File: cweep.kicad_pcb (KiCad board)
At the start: 2 copper layers, 106.6 x 82.7 mm, 57 parts

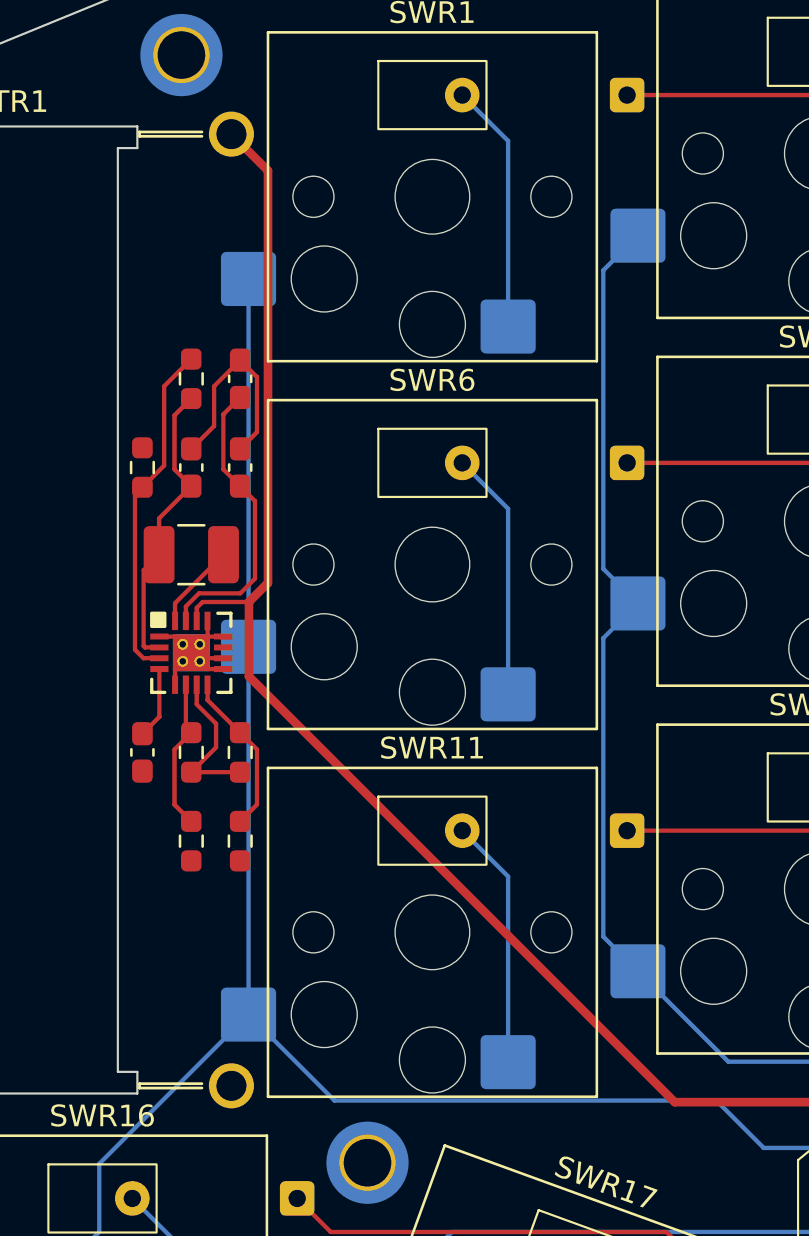
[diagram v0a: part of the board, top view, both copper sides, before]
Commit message: feat: add solar cell connectors
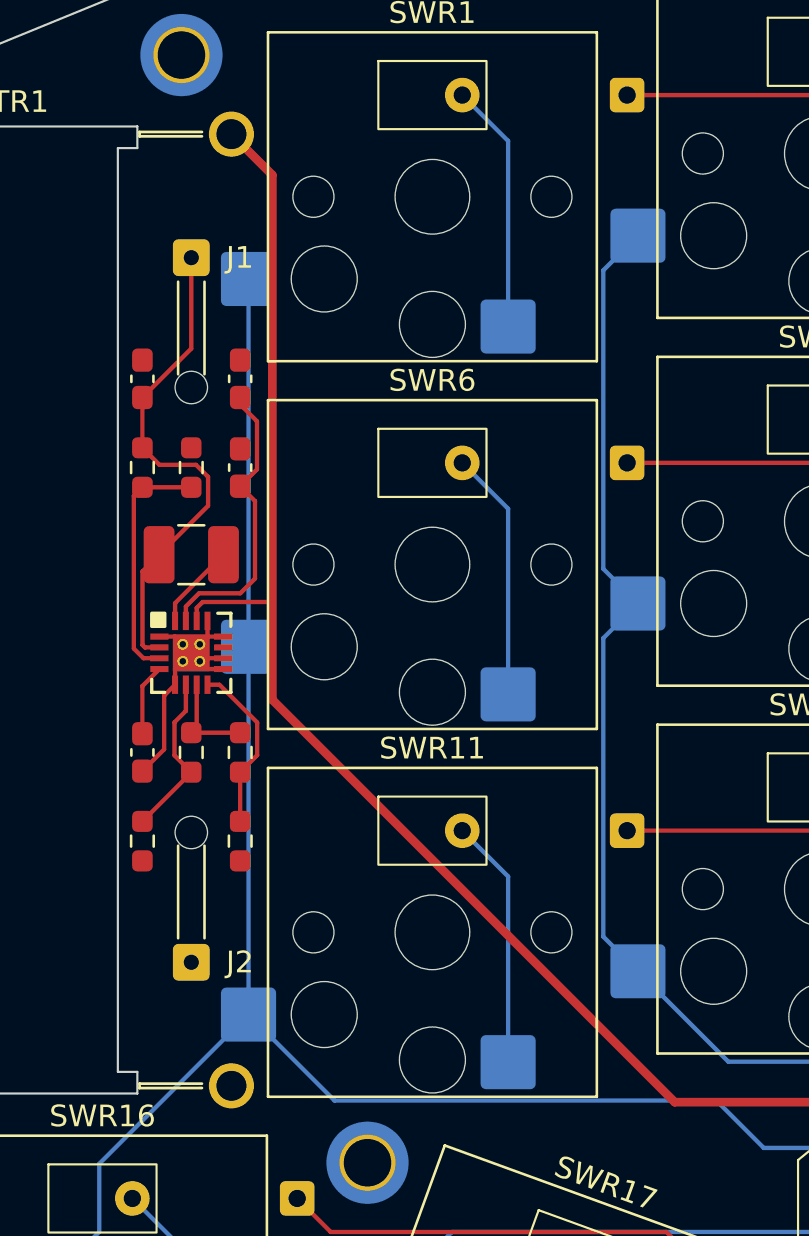
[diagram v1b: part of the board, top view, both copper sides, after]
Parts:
- added J1: 24AWG Hole, Connector_Wire:SolderWire-0.127sqmm_1x01_D0.48mm_OD1mm_Relief, F.Cu at (175.9, 53.8)
- added J2: 24AWG Hole, Connector_Wire:SolderWire-0.127sqmm_1x01_D0.48mm_OD1mm_Relief, F.Cu at (175.9, 86.4)
- moved CHVR1 4.68 mm to (173.6, 59.4)
- moved ROCR2 4.68 mm to (173.6, 63.5), turned to 90 degrees
- moved ROCR1 2.26 mm to (175.9, 63.5)
- moved ROVR1 2.26 mm to (173.6, 80.8)
- turned ROVR2 to 90 degrees
- turned RUVR2 to 90 degrees
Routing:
- net Net-(J1-Pin_1): track 13.7 -> 23.2 mm
- net GND: track 17.1 -> 11.5 mm
- net Net-(UR2-VOC_SAMP): track 15.8 -> 11.2 mm
- net Net-(UR2-VRDIV): track 7.15 -> 4.58 mm
- net Net-(UR2-VBAT_OV): track 7.06 -> 7.79 mm

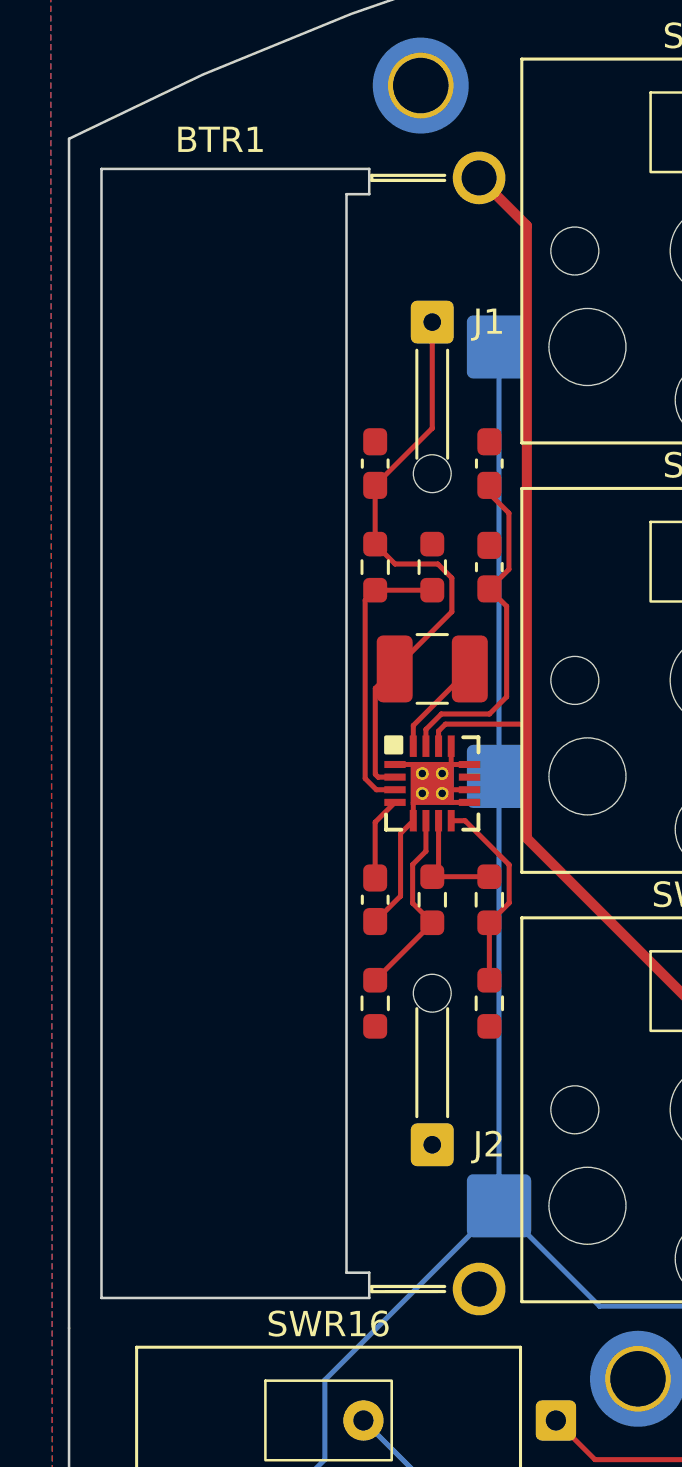
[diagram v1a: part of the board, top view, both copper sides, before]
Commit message: fix: AAA -> 10440
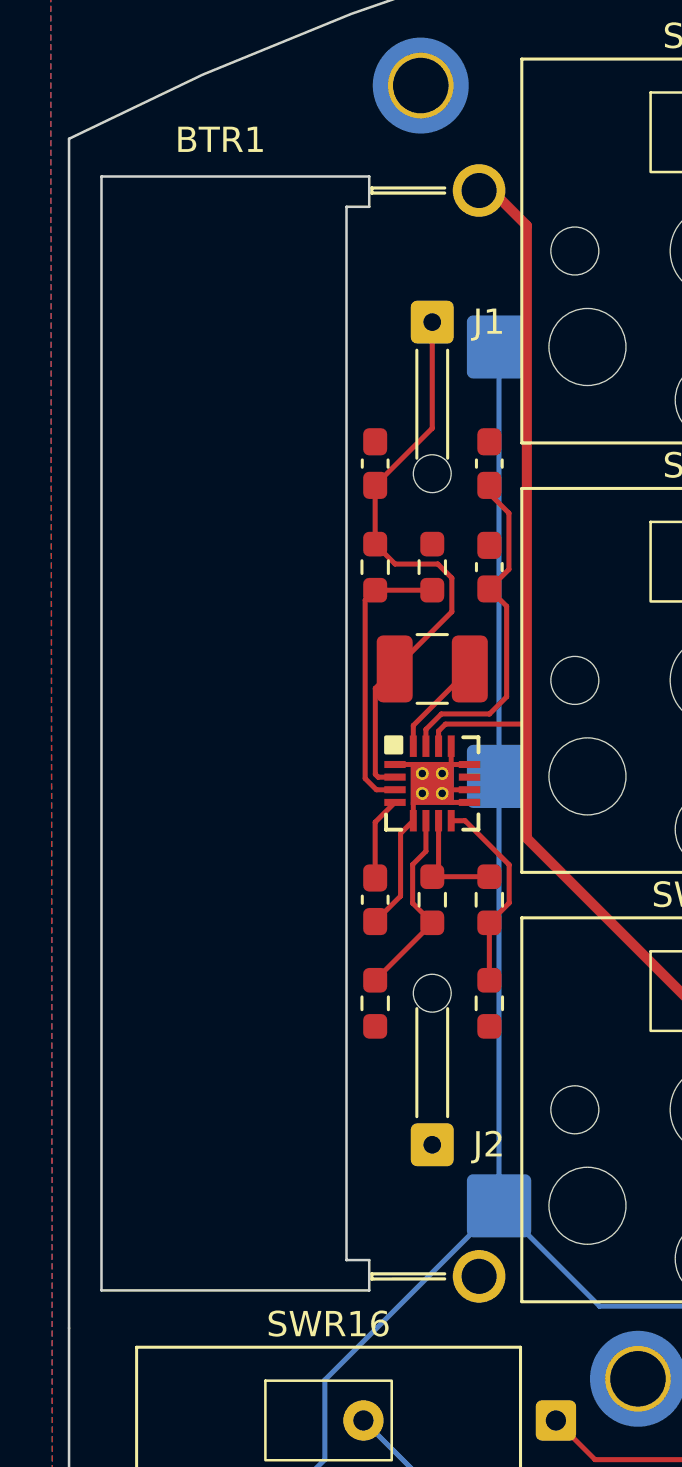
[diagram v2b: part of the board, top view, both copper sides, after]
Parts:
- BTR1: value BATTERY LITH-ION 3.7V AAA -> 10440; footprint com_snapeda_Keystone:BatteryHolder_Keystone_230-1_1xAAA -> com_snapeda_Keystone:BatteryHolder_Keystone_230-1_1x10440

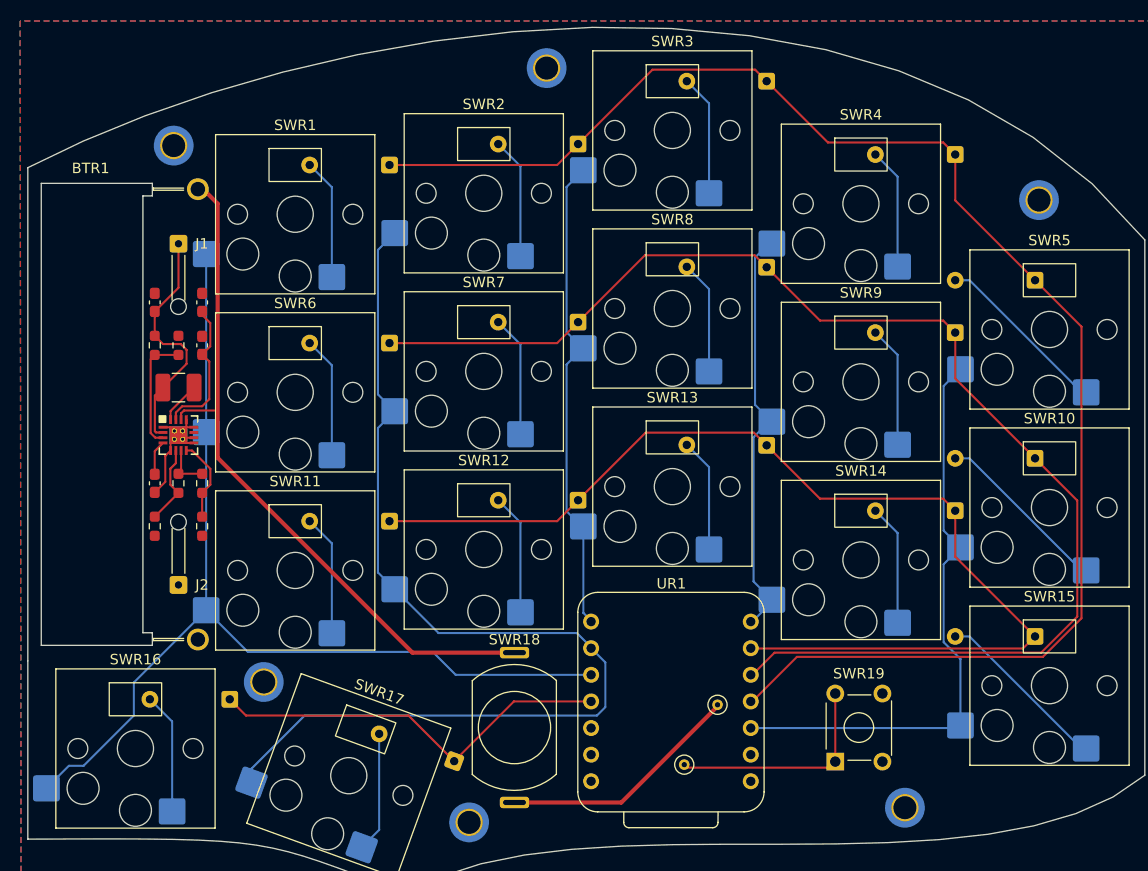
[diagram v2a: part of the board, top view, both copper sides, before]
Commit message: refactor: normalize labels and organize schematic
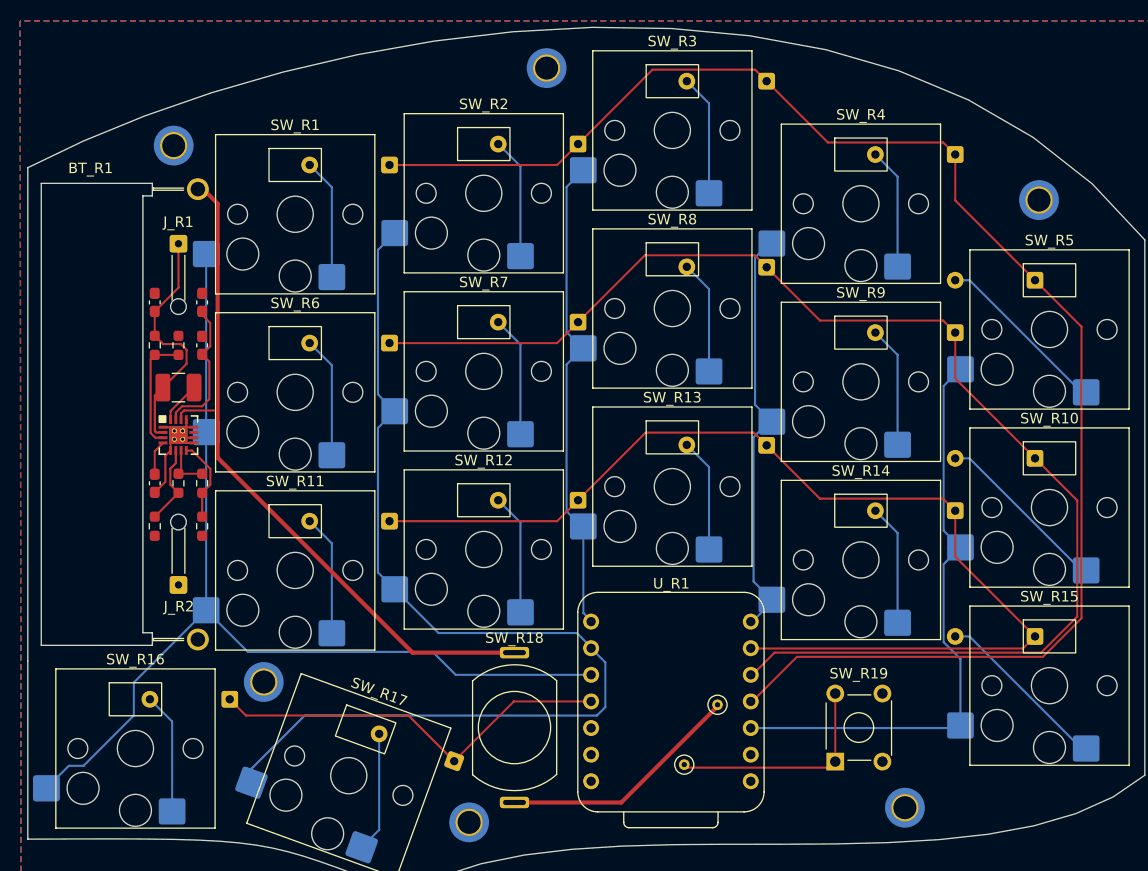
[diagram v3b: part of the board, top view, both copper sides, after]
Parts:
- turned SW_R18 to 180 degrees
- renumbered BTR1 to BT_R1, CBYPR1 to CBYP_R1, CHVR1 to CHV_R1, CREFR1 to CREF_R1, CSTORR1 to CSTOR_R1, DR1 to D_R1, DR10 to D_R10, DR11 to D_R11, DR12 to D_R12, DR13 to D_R13, DR14 to D_R14, DR15 to D_R15, DR16 to D_R16, DR17 to D_R17, DR2 to D_R2, DR3 to D_R3, DR4 to D_R4, DR5 to D_R5, DR6 to D_R6, DR7 to D_R7, DR8 to D_R8, DR9 to D_R9, H1 to H_R1, H2 to H_R2, H3 to H_R3, H4 to H_R4, H5 to H_R5, H6 to H_R6, J1 to J_R1, J2 to J_R2, LBSTR1 to LBST_R1, ROCR1 to ROC_R1, ROCR2 to ROC_R2, ROVR1 to ROV_R1, ROVR2 to ROV_R2, RUVR1 to RUV_R1, RUVR2 to RUV_R2, SCR1 to SC_R1, SWR1 to SW_R1, SWR10 to SW_R10, SWR11 to SW_R11, SWR12 to SW_R12, SWR13 to SW_R13, SWR14 to SW_R14, SWR15 to SW_R15, SWR16 to SW_R16, SWR17 to SW_R17, SWR18 to SW_R18, SWR19 to SW_R19, SWR2 to SW_R2, SWR3 to SW_R3, SWR4 to SW_R4, SWR5 to SW_R5, SWR6 to SW_R6, SWR7 to SW_R7, SWR8 to SW_R8, SWR9 to SW_R9, UR1 to U_R1, UR2 to U_R2
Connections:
- net /column r0 renamed /COL_R0
- net /column r1 renamed /COL_R1
- net /column r2 renamed /COL_R2
- net /column r3 renamed /COL_R3
- net /column r4 renamed /COL_R4
- net /row r0 renamed /ROW_R0
- net /row r1 renamed /ROW_R1
- net /row r2 renamed /ROW_R2
- net /row r3 renamed /ROW_R3
- net Net-(J1-Pin_1) renamed /SOL_R
- net Net-(UR1-RESET) renamed /RST_R
- BT_R1 pad 1: /VBATR -> /VBAT_R
- SW_R18 pad 1: Net-(SWR18-A) -> /VBAT_R
- SW_R18 pad 2: /VBATR -> /BAT_R
- U_R1 pad 15: Net-(SWR18-A) -> /BAT_R
- U_R2 pad 14: /VBATR -> /VBAT_R
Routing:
- net /VBAT_R: track 0.00 -> 67.2 mm
- net /VBATR: track 67.2 -> 0.00 mm
- net Net-(SWR18-A): track 23.3 -> 0.00 mm
- net /BAT_R: track 0.00 -> 23.3 mm

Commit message: feat: make keyboard switch reversible
* fix: use SMD diode to accommodate reversible switch
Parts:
- added JP1: SolderJumper_3_Open, cweep:SolderJumper-3_P2.0mm_Open_TrianglePad1.0x1.5mm_Reversible, F.Cu at (79.3, 84.7)
- added JP10: SolderJumper_3_Open, cweep:SolderJumper-3_P2.0mm_Open_TrianglePad1.0x1.5mm_Reversible, F.Cu at (69.2, 74.6)
- added JP11: SolderJumper_3_Open, cweep:SolderJumper-3_P2.0mm_Open_TrianglePad1.0x1.5mm_Reversible, F.Cu at (72.3, 77.1)
- added JP12: SolderJumper_3_Open, cweep:SolderJumper-3_P2.0mm_Open_TrianglePad1.0x1.5mm_Reversible, F.Cu at (69.2, 79.6)
- added JP13: SolderJumper_3_Open, cweep:SolderJumper-3_P2.0mm_Open_TrianglePad1.0x1.5mm_Reversible, F.Cu at (69.2, 82.2)
- added JP14: SolderJumper_3_Open, cweep:SolderJumper-3_P2.0mm_Open_TrianglePad1.0x1.5mm_Reversible, F.Cu at (69.2, 84.7)
- added JP2: SolderJumper_3_Open, cweep:SolderJumper-3_P2.0mm_Open_TrianglePad1.0x1.5mm_Reversible, F.Cu at (79.3, 82.2)
- added JP3: SolderJumper_3_Open, cweep:SolderJumper-3_P2.0mm_Open_TrianglePad1.0x1.5mm_Reversible, F.Cu at (79.3, 79.6)
- added JP4: SolderJumper_3_Open, cweep:SolderJumper-3_P2.0mm_Open_TrianglePad1.0x1.5mm_Reversible, F.Cu at (76.3, 77.1)
- added JP5: SolderJumper_3_Open, cweep:SolderJumper-3_P2.0mm_Open_TrianglePad1.0x1.5mm_Reversible, F.Cu at (79.3, 74.6)
- added JP6: SolderJumper_3_Open, cweep:SolderJumper-3_P2.0mm_Open_TrianglePad1.0x1.5mm_Reversible, F.Cu at (79.3, 72.0)
- added JP7: SolderJumper_3_Open, cweep:SolderJumper-3_P2.0mm_Open_TrianglePad1.0x1.5mm_Reversible, F.Cu at (79.3, 69.5)
- added JP8: SolderJumper_3_Open, cweep:SolderJumper-3_P2.0mm_Open_TrianglePad1.0x1.5mm_Reversible, F.Cu at (69.2, 69.5)
- added JP9: SolderJumper_3_Open, cweep:SolderJumper-3_P2.0mm_Open_TrianglePad1.0x1.5mm_Reversible, F.Cu at (69.2, 72.0)
- D1: renamed from D_R1; value 1N4148 -> 1N4148W; footprint Diode_THT:D_DO-35_SOD27_P7.62mm_Horizontal -> cweep:D_SOD-123_Reversible; moved to F.Cu
- D10: renamed from D_R10; value 1N4148 -> 1N4148W; footprint Diode_THT:D_DO-35_SOD27_P7.62mm_Horizontal -> cweep:D_SOD-123_Reversible; moved to F.Cu
- D11: renamed from D_R11; value 1N4148 -> 1N4148W; footprint Diode_THT:D_DO-35_SOD27_P7.62mm_Horizontal -> cweep:D_SOD-123_Reversible; moved to F.Cu
- D12: renamed from D_R12; value 1N4148 -> 1N4148W; footprint Diode_THT:D_DO-35_SOD27_P7.62mm_Horizontal -> cweep:D_SOD-123_Reversible; moved to F.Cu
- D13: renamed from D_R13; value 1N4148 -> 1N4148W; footprint Diode_THT:D_DO-35_SOD27_P7.62mm_Horizontal -> cweep:D_SOD-123_Reversible; moved to F.Cu
- D14: renamed from D_R14; value 1N4148 -> 1N4148W; footprint Diode_THT:D_DO-35_SOD27_P7.62mm_Horizontal -> cweep:D_SOD-123_Reversible; moved to F.Cu
- D15: renamed from D_R15; value 1N4148 -> 1N4148W; footprint Diode_THT:D_DO-35_SOD27_P7.62mm_Horizontal -> cweep:D_SOD-123_Reversible; moved to F.Cu
- D16: renamed from D_R16; value 1N4148 -> 1N4148W; footprint Diode_THT:D_DO-35_SOD27_P7.62mm_Horizontal -> cweep:D_SOD-123_Reversible; moved to F.Cu
- D17: renamed from D_R17; value 1N4148 -> 1N4148W; footprint Diode_THT:D_DO-35_SOD27_P7.62mm_Horizontal -> cweep:D_SOD-123_Reversible; moved to F.Cu
- D2: renamed from D_R2; value 1N4148 -> 1N4148W; footprint Diode_THT:D_DO-35_SOD27_P7.62mm_Horizontal -> cweep:D_SOD-123_Reversible; moved to F.Cu
- D3: renamed from D_R3; value 1N4148 -> 1N4148W; footprint Diode_THT:D_DO-35_SOD27_P7.62mm_Horizontal -> cweep:D_SOD-123_Reversible; moved to F.Cu
- D4: renamed from D_R4; value 1N4148 -> 1N4148W; footprint Diode_THT:D_DO-35_SOD27_P7.62mm_Horizontal -> cweep:D_SOD-123_Reversible; moved to F.Cu
- D5: renamed from D_R5; value 1N4148 -> 1N4148W; footprint Diode_THT:D_DO-35_SOD27_P7.62mm_Horizontal -> cweep:D_SOD-123_Reversible; moved to F.Cu
- D6: renamed from D_R6; value 1N4148 -> 1N4148W; footprint Diode_THT:D_DO-35_SOD27_P7.62mm_Horizontal -> cweep:D_SOD-123_Reversible; moved to F.Cu
- D7: renamed from D_R7; value 1N4148 -> 1N4148W; footprint Diode_THT:D_DO-35_SOD27_P7.62mm_Horizontal -> cweep:D_SOD-123_Reversible; moved to F.Cu
- D8: renamed from D_R8; value 1N4148 -> 1N4148W; footprint Diode_THT:D_DO-35_SOD27_P7.62mm_Horizontal -> cweep:D_SOD-123_Reversible; moved to F.Cu
- D9: renamed from D_R9; value 1N4148 -> 1N4148W; footprint Diode_THT:D_DO-35_SOD27_P7.62mm_Horizontal -> cweep:D_SOD-123_Reversible; moved to F.Cu
- SW1: renamed from SW_R1; footprint Switch_Keyboard_Hotswap_Kailh:SW_Hotswap_Kailh_Choc_V1_1.00u -> cweep:SW_Hotswap_Kailh_Choc_V1_1.00u_Reversible
- SW10: renamed from SW_R10; footprint Switch_Keyboard_Hotswap_Kailh:SW_Hotswap_Kailh_Choc_V1_1.00u -> cweep:SW_Hotswap_Kailh_Choc_V1_1.00u_Reversible
- SW11: renamed from SW_R11; footprint Switch_Keyboard_Hotswap_Kailh:SW_Hotswap_Kailh_Choc_V1_1.00u -> cweep:SW_Hotswap_Kailh_Choc_V1_1.00u_Reversible
- SW12: renamed from SW_R12; footprint Switch_Keyboard_Hotswap_Kailh:SW_Hotswap_Kailh_Choc_V1_1.00u -> cweep:SW_Hotswap_Kailh_Choc_V1_1.00u_Reversible
- SW13: renamed from SW_R13; footprint Switch_Keyboard_Hotswap_Kailh:SW_Hotswap_Kailh_Choc_V1_1.00u -> cweep:SW_Hotswap_Kailh_Choc_V1_1.00u_Reversible
- SW14: renamed from SW_R14; footprint Switch_Keyboard_Hotswap_Kailh:SW_Hotswap_Kailh_Choc_V1_1.00u -> cweep:SW_Hotswap_Kailh_Choc_V1_1.00u_Reversible
- SW15: renamed from SW_R15; footprint Switch_Keyboard_Hotswap_Kailh:SW_Hotswap_Kailh_Choc_V1_1.00u -> cweep:SW_Hotswap_Kailh_Choc_V1_1.00u_Reversible
- SW16: renamed from SW_R16; footprint Switch_Keyboard_Hotswap_Kailh:SW_Hotswap_Kailh_Choc_V1_1.00u -> cweep:SW_Hotswap_Kailh_Choc_V1_1.00u_Reversible
- SW17: renamed from SW_R17; footprint Switch_Keyboard_Hotswap_Kailh:SW_Hotswap_Kailh_Choc_V1_1.00u -> cweep:SW_Hotswap_Kailh_Choc_V1_1.00u_Reversible
- SW2: renamed from SW_R2; footprint Switch_Keyboard_Hotswap_Kailh:SW_Hotswap_Kailh_Choc_V1_1.00u -> cweep:SW_Hotswap_Kailh_Choc_V1_1.00u_Reversible
- SW3: renamed from SW_R3; footprint Switch_Keyboard_Hotswap_Kailh:SW_Hotswap_Kailh_Choc_V1_1.00u -> cweep:SW_Hotswap_Kailh_Choc_V1_1.00u_Reversible
- SW4: renamed from SW_R4; footprint Switch_Keyboard_Hotswap_Kailh:SW_Hotswap_Kailh_Choc_V1_1.00u -> cweep:SW_Hotswap_Kailh_Choc_V1_1.00u_Reversible
- SW5: renamed from SW_R5; footprint Switch_Keyboard_Hotswap_Kailh:SW_Hotswap_Kailh_Choc_V1_1.00u -> cweep:SW_Hotswap_Kailh_Choc_V1_1.00u_Reversible
- SW6: renamed from SW_R6; footprint Switch_Keyboard_Hotswap_Kailh:SW_Hotswap_Kailh_Choc_V1_1.00u -> cweep:SW_Hotswap_Kailh_Choc_V1_1.00u_Reversible
- SW7: renamed from SW_R7; footprint Switch_Keyboard_Hotswap_Kailh:SW_Hotswap_Kailh_Choc_V1_1.00u -> cweep:SW_Hotswap_Kailh_Choc_V1_1.00u_Reversible
- SW8: renamed from SW_R8; footprint Switch_Keyboard_Hotswap_Kailh:SW_Hotswap_Kailh_Choc_V1_1.00u -> cweep:SW_Hotswap_Kailh_Choc_V1_1.00u_Reversible
- SW9: renamed from SW_R9; footprint Switch_Keyboard_Hotswap_Kailh:SW_Hotswap_Kailh_Choc_V1_1.00u -> cweep:SW_Hotswap_Kailh_Choc_V1_1.00u_Reversible
- moved D13 159.0 mm to (74.4, 51.9), turned to 0.3 degrees
- moved D8 159.0 mm to (74.4, 34.9), turned to 0.3 degrees
- moved D1 158.9 mm to (38.4, 25.9), turned to 0 degrees
- moved D11 158.9 mm to (38.4, 59.9), turned to 0 degrees
- moved D12 158.9 mm to (56.4, 57.9), turned to 0 degrees
- moved D14 158.9 mm to (92.4, 58.9), turned to 0 degrees
- moved D2 158.9 mm to (56.4, 23.9), turned to 0 degrees
- moved D3 158.9 mm to (74.4, 17.9), turned to 0 degrees
- moved D4 158.9 mm to (92.4, 24.9), turned to 0 degrees
- moved D6 158.9 mm to (38.4, 42.9), turned to 0 degrees
- moved D7 158.9 mm to (56.4, 40.9), turned to 0 degrees
- moved D9 158.9 mm to (92.4, 41.9), turned to 0 degrees
- moved D16 158.9 mm to (23.1, 76.9), turned to 0 degrees
- moved D17 158.8 mm to (45.1, 79.8), turned to -20 degrees
- moved SW17 150.0 mm to (43.5, 84.2)
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- renumbered BT_R1 to BT1, CBYP_R1 to CBYP1, CHV_R1 to CHV1, CREF_R1 to CREF1, CSTOR_R1 to CSTOR1, H_R1 to H1, H_R2 to H2, H_R3 to H3, H_R4 to H4, H_R5 to H5, H_R6 to H6, J_R1 to J1, J_R2 to J2, LBST_R1 to LBST1, ROC_R1 to ROC1, ROC_R2 to ROC2, ROV_R1 to ROV1, ROV_R2 to ROV2, RUV_R1 to RUV1, RUV_R2 to RUV2, SC_R1 to SC1, SW_R18 to SW18, SW_R19 to SW19, U_R1 to U1, U_R2 to U2
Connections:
- net /BAT_R renamed /BAT
- net /RST_R renamed /RST
- net /SOL_R renamed /SOL
- net /VBAT_R renamed /VBAT
- D1 pad 1: /ROW_R0 -> /ROW0
- D10 pad 1: /ROW_R1 -> /ROW1
- D11 pad 1: /ROW_R2 -> /ROW2
- D12 pad 1: /ROW_R2 -> /ROW2
- D13 pad 1: /ROW_R2 -> /ROW2
- D14 pad 1: /ROW_R2 -> /ROW2
- D15 pad 1: /ROW_R2 -> /ROW2
- D16 pad 1: /ROW_R3 -> /ROW3
- D17 pad 1: /ROW_R3 -> /ROW3
- D2 pad 1: /ROW_R0 -> /ROW0
- D3 pad 1: /ROW_R0 -> /ROW0
- D4 pad 1: /ROW_R0 -> /ROW0
- D5 pad 1: /ROW_R0 -> /ROW0
- D6 pad 1: /ROW_R1 -> /ROW1
- D7 pad 1: /ROW_R1 -> /ROW1
- D8 pad 1: /ROW_R1 -> /ROW1
- D9 pad 1: /ROW_R1 -> /ROW1
- SW1 pad 1: /COL_R0 -> /COL0
- SW10 pad 1: /COL_R4 -> /COL4
- SW11 pad 1: /COL_R0 -> /COL0
- SW12 pad 1: /COL_R1 -> /COL1
- SW13 pad 1: /COL_R2 -> /COL2
- SW14 pad 1: /COL_R3 -> /COL3
- SW15 pad 1: /COL_R4 -> /COL4
- SW16 pad 1: /COL_R0 -> /COL0
- SW17 pad 1: /COL_R1 -> /COL1
- SW2 pad 1: /COL_R1 -> /COL1
- SW3 pad 1: /COL_R2 -> /COL2
- SW4 pad 1: /COL_R3 -> /COL3
- SW5 pad 1: /COL_R4 -> /COL4
- SW6 pad 1: /COL_R0 -> /COL0
- SW7 pad 1: /COL_R1 -> /COL1
- SW8 pad 1: /COL_R2 -> /COL2
- SW9 pad 1: /COL_R3 -> /COL3
- U1 pad 1: unconnected-(U_R1-P0.02_A0_D0-Pad1) -> /PIN1
- U1 pad 10: /COL_R0 -> /PIN10
- U1 pad 11: /ROW_R3 -> /PIN11
- U1 pad 12: unconnected-(U_R1-3V3-Pad12) -> /PIN12
- U1 pad 13: GND -> /PIN13
- U1 pad 14: unconnected-(U_R1-5V-Pad14) -> /PIN14
- U1 pad 2: unconnected-(U_R1-P0.03_A1_D1-Pad2) -> /PIN2
- U1 pad 3: /COL_R4 -> /PIN3
- U1 pad 4: /ROW_R0 -> /PIN4
- U1 pad 5: /ROW_R1 -> /PIN5
- U1 pad 6: /ROW_R2 -> /PIN6
- U1 pad 7: /COL_R3 -> /PIN7
- U1 pad 8: /COL_R2 -> /PIN8
- U1 pad 9: /COL_R1 -> /PIN9
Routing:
- net /COL0: track 0.00 -> 152.8 mm
- net /ROW_R0: track 145.5 -> 0.00 mm
- net /COL1: track 0.00 -> 138.9 mm
- net /ROW_R1: track 126.2 -> 0.00 mm
- net /COL4: track 0.00 -> 108.2 mm
- net /ROW_R2: track 103.2 -> 0.00 mm
- net /COL_R1: track 101.6 -> 0.00 mm
- net /ROW2: track 0.00 -> 99.0 mm
- net /COL_R0: track 97.4 -> 0.00 mm
- net /COL2: track 0.00 -> 94.4 mm
- net /COL3: track 0.00 -> 90.3 mm
- net /ROW0: track 0.00 -> 83.4 mm
- net /ROW1: track 0.00 -> 83.4 mm
- net /COL_R4: track 56.8 -> 0.00 mm
- net /VBAT: track 67.2 -> 16.6 mm
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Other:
- board size 106.6 x 82.7 mm -> 108 x 82.5 mm
